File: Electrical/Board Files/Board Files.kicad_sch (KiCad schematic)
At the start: 7 parts

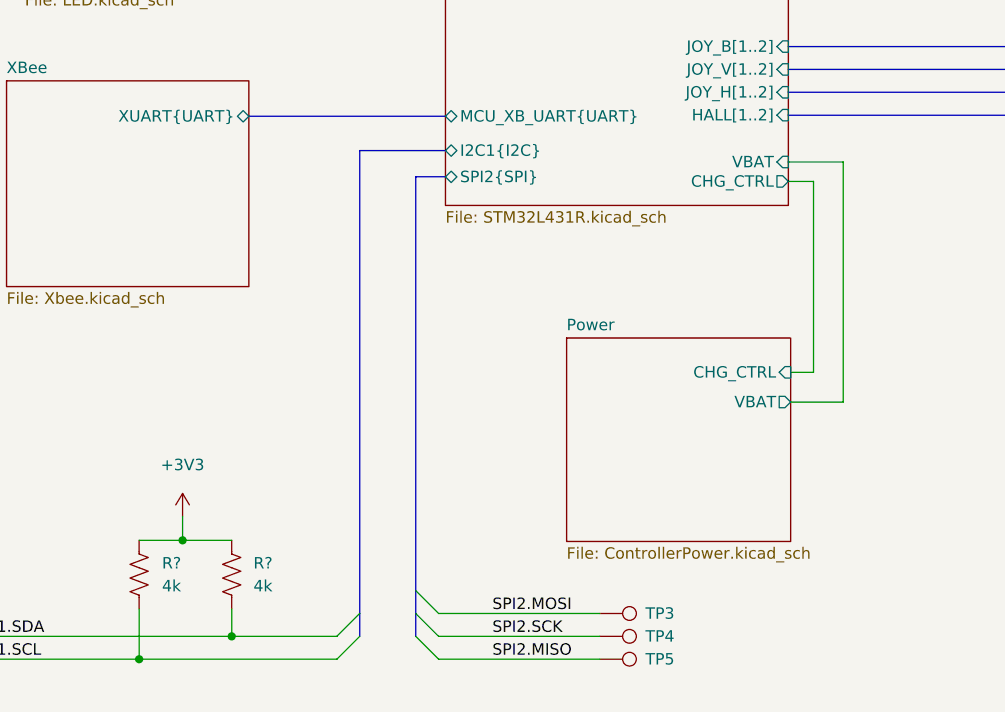
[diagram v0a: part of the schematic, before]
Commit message: Fixing USB pins and added SPI_CS
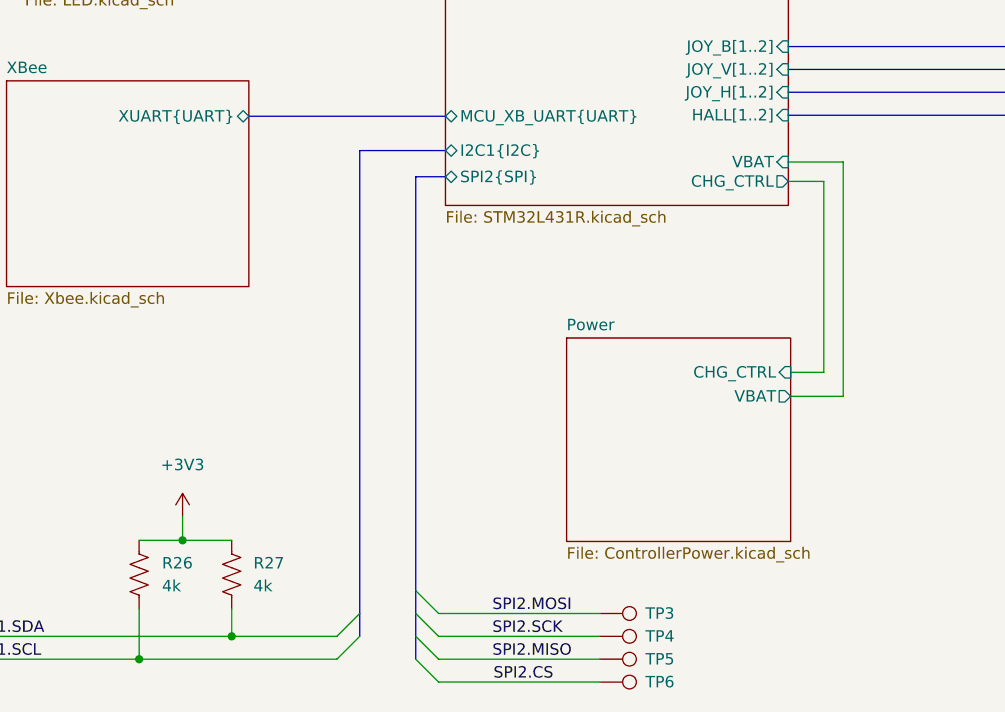
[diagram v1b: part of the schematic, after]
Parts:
- added TP6: ~, symbol Connector:TestPoint
- gave numbers to parts that had none: 2
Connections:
- new net SPI2.CS: TP6.1
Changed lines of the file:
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@@
   (junction (at 80.01 169.037) (diameter 0) (color 0 0 0 0)
   )
+  (bus_entry (at 110.744 169.037) (size 2.54 2.54)
+    (stroke (width 0) (type default) (color 0 0 0 0))
+  )
   (bus_entry (at 110.744 161.417) (size 2.54 2.54)
     (stroke (width 0) (type default) (color 0 0 0 0))
@@
     (stroke (width 0) (type default) (color 0 0 0 0))
   )
-  (wire (pts (xy 158.242 113.792) (xy 158.242 140.462))
+  (wire (pts (xy 158.242 113.792) (xy 158.242 139.827))
     (stroke (width 0) (type default) (color 0 0 0 0))
   )
@@
     (stroke (width 0) (type default) (color 0 0 0 0))
   )
+  (bus (pts (xy 110.744 166.497) (xy 110.744 169.037))
+    (stroke (width 0) (type default) (color 0 0 0 0))
+  )
   (wire (pts (xy 90.297 163.449) (xy 90.297 166.497))
     (stroke (width 0) (type default) (color 0 0 0 0))
@@
     (stroke (width 0) (type default) (color 0 0 0 0))
   )
-  (wire (pts (xy 152.4 137.16) (xy 154.94 137.16))
-    (stroke (width 0) (type default) (color 0 0 0 0))
-  )
-  (wire (pts (xy 154.94 137.16) (xy 154.94 115.951))
+  (wire (pts (xy 152.4 137.16) (xy 156.083 137.16))
+    (stroke (width 0) (type default) (color 0 0 0 0))
+  )
+  (wire (pts (xy 156.083 137.16) (xy 156.083 115.951))
     (stroke (width 0) (type default) (color 0 0 0 0))
   )
@@
     (stroke (width 0) (type default) (color 0 0 0 0))
   )
+  (wire (pts (xy 113.284 171.577) (xy 131.191 171.577))
+    (stroke (width 0) (type default) (color 0 0 0 0))
+  )
   (bus (pts (xy 93.218 90.551) (xy 114.046 90.551))
     (stroke (width 0) (type default) (color 0 0 0 0))
@@
     (stroke (width 0) (type default) (color 0 0 0 0))
   )
-  (wire (pts (xy 154.94 115.951) (xy 152.146 115.951))
-    (stroke (width 0) (type default) (color 0 0 0 0))
-  )
-  (wire (pts (xy 158.242 140.462) (xy 152.4 140.462))
+  (wire (pts (xy 156.083 115.951) (xy 152.146 115.951))
+    (stroke (width 0) (type default) (color 0 0 0 0))
+  )
+  (wire (pts (xy 158.242 139.827) (xy 152.4 139.827))
     (stroke (width 0) (type default) (color 0 0 0 0))
   )
@@
   (bus (pts (xy 152.146 100.965) (xy 187.198 100.965))
     (stroke (width 0) (type default) (color 0 0 0 0))
+  )
+  (label "SPI2.CS" (at 119.38 171.577 0)
+    (effects (font (size 1.27 1.27)) (justify left bottom))
   )
   (label "SPI2.MOSI" (at 119.253 163.957 0)
@@
   (symbol (lib_id "Device:R_US") (at 90.297 159.639 0) (unit 1)
     (in_bom yes) (on_board yes) (fields_autoplaced)
-    (property "Reference" "R?" (id 0) (at 92.71 158.3689 0)
+    (property "Reference" "R27" (id 0) (at 92.71 158.3689 0)
       (effects (font (size 1.27 1.27)) (justify left))
     )
@@
     (pin "2")
   )
+  (symbol (lib_id "Connector:TestPoint") (at 131.191 171.577 270) (unit 1)
+    (in_bom yes) (on_board yes)
+    (property "Reference" "TP6" (id 0) (at 136.271 171.5769 90)
+      (effects (font (size 1.27 1.27)) (justify left))
+    )
+    (property "Value" "~" (id 1) (at 136.271 172.8469 90)
+      (effects (font (size 1.27 1.27)) (justify left))
+    )
+    (property "Footprint" "" (id 2) (at 131.191 176.657 0)
+      (effects (font (size 1.27 1.27)) hide)
+    )
+    (property "Datasheet" "~" (id 3) (at 131.191 176.657 0)
+      (effects (font (size 1.27 1.27)) hide)
+    )
+    (pin "1")
+  )
   (symbol (lib_id "power:+3V3") (at 84.836 153.162 0) (unit 1)
     (in_bom yes) (on_board yes) (fields_autoplaced)
-    (property "Reference" "#PWR?" (id 0) (at 84.836 156.972 0)
+    (property "Reference" "#PWR0101" (id 0) (at 84.836 156.972 0)
       (effects (font (size 1.27 1.27)) hide)
     )
@@
   (symbol (lib_id "Device:R_US") (at 80.01 159.639 0) (unit 1)
     (in_bom yes) (on_board yes) (fields_autoplaced)
-    (property "Reference" "R?" (id 0) (at 82.55 158.3689 0)
+    (property "Reference" "R26" (id 0) (at 82.55 158.3689 0)
       (effects (font (size 1.27 1.27)) (justify left))
     )
@@
       (effects (font (size 1.27 1.27)) (justify right))
     )
-    (pin "VBAT" output (at 152.4 140.462 0)
+    (pin "VBAT" output (at 152.4 139.827 0)
       (effects (font (size 1.27 1.27)) (justify right))
     )
@@
     )
     (path "/7cc79bd2-039f-416d-bb6d-e5ab625e9395"
-      (reference "#PWR?") (unit 1) (value "+3V3") (footprint "")
+      (reference "#PWR0101") (unit 1) (value "+3V3") (footprint "")
     )
     (path "/be02c95d-2968-40ec-875d-106e3ff13333/6ef1c94a-5d04-44b4-8be3-ff213f767449"
@@
       (reference "J1") (unit 1) (value "Conn_01x02_Female") (footprint "")
     )
-    (path "/e09ee552-eb48-4e80-8b06-29cfae21f4b7/e1671fc6-5fe7-445e-99c8-dfb3e26931be"
-      (reference "J2") (unit 1) (value "Conn_01x04_Female") (footprint "")
+    (path "/e09ee552-eb48-4e80-8b06-29cfae21f4b7/bcf54167-50e1-4b8c-92a2-d5c4cc6dee15"
+      (reference "J2") (unit 1) (value "Conn_01x05_Female") (footprint "")
     )
     (path "/e09ee552-eb48-4e80-8b06-29cfae21f4b7/f3eff741-c4bc-4f9a-9425-14ce9c96edba"
@@
     )
     (path "/be02c95d-2968-40ec-875d-106e3ff13333/868ce63c-af2d-488a-b499-97eadbcb8b55"
-      (reference "R10") (unit 1) (value "R_US") (footprint "")
+      (reference "R10") (unit 1) (value "10k") (footprint "")
     )
     (path "/be02c95d-2968-40ec-875d-106e3ff13333/cc200e16-9ba2-4cb0-bf5f-b752532581c8"
@@
     )
     (path "/be02c95d-2968-40ec-875d-106e3ff13333/580c251f-a4c1-4f08-a916-eb6ecbb2ef0a"
-      (reference "R14") (unit 1) (value "R_US") (footprint "")
+      (reference "R14") (unit 1) (value "10k") (footprint "")
     )
     (path "/be02c95d-2968-40ec-875d-106e3ff13333/7244af40-f453-40af-8e71-efad98265674"
@@
       (reference "R25") (unit 1) (value "270R") (footprint "")
     )
+    (path "/f4afd273-67bb-42af-9506-6bcff6f56d65"
+      (reference "R26") (unit 1) (value "4k") (footprint "")
+    )
     (path "/28bacfba-e192-4f1a-bb0f-2d223f49ce66"
-      (reference "R?") (unit 1) (value "4k") (footprint "")
-    )
-    (path "/f4afd273-67bb-42af-9506-6bcff6f56d65"
-      (reference "R?") (unit 1) (value "4k") (footprint "")
+      (reference "R27") (unit 1) (value "4k") (footprint "")
     )
     (path "/e322e877-fa4b-40a1-b9eb-04bd2db5ed6c/3de267d4-c1ac-49b4-9115-da53f4d7c2c5"
@@
       (reference "TP5") (unit 1) (value "~") (footprint "")
     )
+    (path "/796256cc-991e-4227-afda-b696eb2e006a"
+      (reference "TP6") (unit 1) (value "~") (footprint "")
+    )
     (path "/899d6960-0494-4e8f-9091-802503c02d1b/7d042535-a9b1-4541-bdce-2605e3a8d022"

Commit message: Adding some device footprints and MPN
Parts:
- R26, R27: footprint (none) -> Resistor_SMD:R_0603_1608Metric
- TP1, TP2, TP4, TP5, TP6: value ~ -> TestPoint; footprint (none) -> TestPoint:TestPoint_THTPad_2.0x2.0mm_Drill1.0mm
- TP3: footprint (none) -> TestPoint:TestPoint_THTPad_2.0x2.0mm_Drill1.0mm

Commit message: No clue what changed
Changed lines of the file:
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@@
     )
     (property "Value" "TestPoint" (id 1) (at 53.213 170.3069 90)
-      (effects (font (size 1.27 1.27)) (justify left))
+      (effects (font (size 1.27 1.27)) (justify left) hide)
     )
     (property "Footprint" "TestPoint:TestPoint_THTPad_2.0x2.0mm_Drill1.0mm" (id 2) (at 58.293 174.117 0)
@@
     )
     (property "Value" "TestPoint" (id 1) (at 136.271 172.8469 90)
-      (effects (font (size 1.27 1.27)) (justify left))
+      (effects (font (size 1.27 1.27)) (justify left) hide)
     )
     (property "Footprint" "TestPoint:TestPoint_THTPad_2.0x2.0mm_Drill1.0mm" (id 2) (at 131.191 176.657 0)
@@
     )
     (property "Value" "TestPoint" (id 1) (at 136.271 170.3069 90)
-      (effects (font (size 1.27 1.27)) (justify left))
+      (effects (font (size 1.27 1.27)) (justify left) hide)
     )
     (property "Footprint" "TestPoint:TestPoint_THTPad_2.0x2.0mm_Drill1.0mm" (id 2) (at 131.191 174.117 0)
@@
     )
     (property "Value" "TestPoint" (id 1) (at 53.213 167.7669 90)
-      (effects (font (size 1.27 1.27)) (justify left))
+      (effects (font (size 1.27 1.27)) (justify left) hide)
     )
     (property "Footprint" "TestPoint:TestPoint_THTPad_2.0x2.0mm_Drill1.0mm" (id 2) (at 58.293 171.577 0)
@@
     )
     (property "Value" "TestPoint" (id 1) (at 136.271 167.7669 90)
-      (effects (font (size 1.27 1.27)) (justify left))
+      (effects (font (size 1.27 1.27)) (justify left) hide)
     )
     (property "Footprint" "TestPoint:TestPoint_THTPad_2.0x2.0mm_Drill1.0mm" (id 2) (at 131.191 171.577 0)
@@
       (reference "#PWR0101") (unit 1) (value "+3V3") (footprint "")
     )
+    (path "/e322e877-fa4b-40a1-b9eb-04bd2db5ed6c/18ffb899-3e45-4805-a8f1-9ae2dcae6953"
+      (reference "#PWR?") (unit 1) (value "GND") (footprint "")
+    )
+    (path "/e09ee552-eb48-4e80-8b06-29cfae21f4b7/30c50e6a-c070-4733-b3f4-4f88267487da"
+      (reference "#PWR?") (unit 1) (value "VBUS") (footprint "")
+    )
+    (path "/e322e877-fa4b-40a1-b9eb-04bd2db5ed6c/93e9e0ab-e3df-4319-ae5d-5928cc54c4dd"
+      (reference "#PWR?") (unit 1) (value "GND") (footprint "")
+    )
+    (path "/e09ee552-eb48-4e80-8b06-29cfae21f4b7/c47211c6-b9de-4e82-aca5-2f2c37d85699"
+      (reference "#PWR?") (unit 1) (value "~") (footprint "")
+    )
+    (path "/e322e877-fa4b-40a1-b9eb-04bd2db5ed6c/d9d83ef2-368c-44ab-9aee-7a4aee403a3f"
+      (reference "#PWR?") (unit 1) (value "GND") (footprint "")
+    )
     (path "/be02c95d-2968-40ec-875d-106e3ff13333/6ef1c94a-5d04-44b4-8be3-ff213f767449"
       (reference "BZ1") (unit 1) (value "Buzzer") (footprint "")
@@
       (reference "C40") (unit 1) (value "0.01u") (footprint "Capacitor_SMD:C_0603_1608Metric")
     )
+    (path "/e09ee552-eb48-4e80-8b06-29cfae21f4b7/2b00caee-ec22-415f-9bde-95858c02627f"
+      (reference "C?") (unit 1) (value "0.1u") (footprint "")
+    )
+    (path "/e09ee552-eb48-4e80-8b06-29cfae21f4b7/a0e063e6-ae3f-4c38-8410-34b4b5cf44f5"
+      (reference "C?") (unit 1) (value "C") (footprint "")
+    )
     (path "/e322e877-fa4b-40a1-b9eb-04bd2db5ed6c/71ae1396-694c-4f1a-8dbc-510787c9338c"
       (reference "D1") (unit 1) (value " - ") (footprint "Diode_SMD:D_SOD-323")
@@
       (reference "R27") (unit 1) (value "4k") (footprint "Resistor_SMD:R_0603_1608Metric")
     )
+    (path "/e322e877-fa4b-40a1-b9eb-04bd2db5ed6c/0d0fb61f-c32b-4e2c-909e-e344c873a478"
+      (reference "R?") (unit 1) (value "10k") (footprint "")
+    )
+    (path "/e322e877-fa4b-40a1-b9eb-04bd2db5ed6c/15d73994-9d47-4ef5-ae7f-e90d9dd439b9"
+      (reference "R?") (unit 1) (value "10k") (footprint "")
+    )
+    (path "/e322e877-fa4b-40a1-b9eb-04bd2db5ed6c/5f4a6ffe-074c-471b-b07a-dbb73cd5e548"
+      (reference "R?") (unit 1) (value "10k") (footprint "")
+    )
+    (path "/e322e877-fa4b-40a1-b9eb-04bd2db5ed6c/d1d3af60-2569-48ce-9fe3-e29102f1536f"
+      (reference "R?") (unit 1) (value "10k") (footprint "")
+    )
     (path "/e322e877-fa4b-40a1-b9eb-04bd2db5ed6c/3de267d4-c1ac-49b4-9115-da53f4d7c2c5"

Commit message: Adding footprints
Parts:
- renumbered R26 to R1, R27 to R2
